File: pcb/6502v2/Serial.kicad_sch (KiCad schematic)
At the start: 10 parts

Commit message: Finally figured out the address decode logic, hopefully im done for now
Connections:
- net A0: now also U?.13 (RS0)
- net A1: now also U?.14 (RS1)
- net Serial Enable: now reaches U?.2 (CS1)
- net Serial ~{Enable}: now reaches U?.3 (~{CS2})
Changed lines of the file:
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@@
     (effects (font (size 1.27 1.27)) (justify right))
   )
-  (hierarchical_label "A1" (shape input) (at 165.354 62.738 180)
+  (hierarchical_label "A1" (shape input) (at 187.706 65.786 180)
+    (effects (font (size 1.27 1.27)) (justify right))
+  )
+  (hierarchical_label "Serial ~{Enable}" (shape input) (at 187.706 58.166 180)
     (effects (font (size 1.27 1.27)) (justify right))
   )
@@
     (effects (font (size 1.27 1.27)) (justify right))
   )
-  (hierarchical_label "A2" (shape input) (at 165.354 65.278 180)
+  (hierarchical_label "Serial Enable" (shape input) (at 187.706 55.626 180)
     (effects (font (size 1.27 1.27)) (justify right))
   )
@@
     (effects (font (size 1.27 1.27)) (justify right))
   )
-  (hierarchical_label "A3" (shape input) (at 165.354 67.818 180)
-    (effects (font (size 1.27 1.27)) (justify right))
-  )
   (hierarchical_label "D5" (shape bidirectional) (at 187.706 93.726 180)
     (effects (font (size 1.27 1.27)) (justify right))
   )
-  (hierarchical_label "A0" (shape input) (at 165.354 60.198 180)
+  (hierarchical_label "A0" (shape input) (at 187.706 63.246 180)
     (effects (font (size 1.27 1.27)) (justify right))
   )
@@
   (symbol (lib_id "power:GND") (at 107.95 113.284 0) (unit 1)
     (in_bom yes) (on_board yes) (fields_autoplaced)
-    (property "Reference" "#PWR?" (id 0) (at 107.95 119.634 0)
+    (property "Reference" "#PWR0145" (id 0) (at 107.95 119.634 0)
       (effects (font (size 1.27 1.27)) hide)
     )
@@
   (symbol (lib_id "power:GND") (at 31.496 87.376 0) (unit 1)
     (in_bom yes) (on_board yes) (fields_autoplaced)
-    (property "Reference" "#PWR?" (id 0) (at 31.496 93.726 0)
+    (property "Reference" "#PWR0144" (id 0) (at 31.496 93.726 0)
       (effects (font (size 1.27 1.27)) hide)
     )
@@
   (symbol (lib_id "power:GND") (at 248.666 42.926 0) (unit 1)
     (in_bom yes) (on_board yes) (fields_autoplaced)
-    (property "Reference" "#PWR?" (id 0) (at 248.666 49.276 0)
+    (property "Reference" "#PWR0147" (id 0) (at 248.666 49.276 0)
       (effects (font (size 1.27 1.27)) hide)
     )
@@
   (symbol (lib_id "power:GND") (at 202.946 108.966 0) (unit 1)
     (in_bom yes) (on_board yes) (fields_autoplaced)
-    (property "Reference" "#PWR?" (id 0) (at 202.946 115.316 0)
+    (property "Reference" "#PWR0148" (id 0) (at 202.946 115.316 0)
       (effects (font (size 1.27 1.27)) hide)
     )
@@
   (symbol (lib_id "power:+5V") (at 202.946 32.258 0) (unit 1)
     (in_bom yes) (on_board yes) (fields_autoplaced)
-    (property "Reference" "#PWR?" (id 0) (at 202.946 36.068 0)
+    (property "Reference" "#PWR0146" (id 0) (at 202.946 36.068 0)
       (effects (font (size 1.27 1.27)) hide)
     )
@@
   (symbol (lib_id "power:GND") (at 141.224 85.344 0) (unit 1)
     (in_bom yes) (on_board yes) (fields_autoplaced)
-    (property "Reference" "#PWR?" (id 0) (at 141.224 91.694 0)
+    (property "Reference" "#PWR0142" (id 0) (at 141.224 91.694 0)
       (effects (font (size 1.27 1.27)) hide)
     )
@@
   (symbol (lib_id "power:+5V") (at 107.95 51.054 0) (unit 1)
     (in_bom yes) (on_board yes) (fields_autoplaced)
-    (property "Reference" "#PWR?" (id 0) (at 107.95 54.864 0)
-      (effects (font (size 1.27 1.27)) hide)
-    )
+    (property "Reference" "#PWR0143" (id 0) (at 107.95 54.864 0)
+      (effects (font (size 1.27 1.27)) hide)
+    )

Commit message: just working
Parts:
- C1, C2, C3, C4, C5: renamed from C?; footprint (none) -> Capacitor_SMD:C_0805_2012Metric
- J12: renamed from J?; footprint (none) -> Connector_Dsub:DSUB-9_Female_Horizontal_P2.77x2.84mm_EdgePinOffset4.94mm_Housed_MountingHolesOffset7.48mm
- R33: renamed from R?; footprint (none) -> Resistor_SMD:R_0805_2012Metric
- U7: renamed from U?; footprint (none) -> Package_DIP:DIP-16_W7.62mm
- Y1: renamed from Y?; footprint (none) -> Crystal:Crystal_HC49-U_Vertical
- gave numbers to parts that had none: 1
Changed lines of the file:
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@@
   (symbol (lib_id "Device:C_Small") (at 132.334 63.754 0) (unit 1)
     (in_bom yes) (on_board yes) (fields_autoplaced)
-    (property "Reference" "C?" (id 0) (at 135.89 62.4902 0)
+    (property "Reference" "C2" (id 0) (at 135.89 62.4902 0)
       (effects (font (size 1.27 1.27)) (justify left))
     )
@@
       (effects (font (size 1.27 1.27)) (justify left))
     )
-    (property "Footprint" "" (id 2) (at 132.334 63.754 0)
+    (property "Footprint" "Capacitor_SMD:C_0805_2012Metric" (id 2) (at 132.334 63.754 0)
       (effects (font (size 1.27 1.27)) hide)
     )
@@
   (symbol (lib_id "Device:R_Small") (at 224.028 43.942 0) (unit 1)
     (in_bom yes) (on_board yes)
-    (property "Reference" "R?" (id 0) (at 226.06 42.6719 0)
+    (property "Reference" "R33" (id 0) (at 226.06 42.6719 0)
       (effects (font (size 1.27 1.27)) (justify left))
     )
@@
       (effects (font (size 1.27 1.27)) (justify left))
     )
-    (property "Footprint" "" (id 2) (at 224.028 43.942 0)
+    (property "Footprint" "Resistor_SMD:R_0805_2012Metric" (id 2) (at 224.028 43.942 0)
       (effects (font (size 1.27 1.27)) hide)
     )
@@
   (symbol (lib_id "power:GND") (at 107.95 113.284 0) (unit 1)
     (in_bom yes) (on_board yes) (fields_autoplaced)
-    (property "Reference" "#PWR0145" (id 0) (at 107.95 119.634 0)
+    (property "Reference" "#PWR044" (id 0) (at 107.95 119.634 0)
       (effects (font (size 1.27 1.27)) hide)
     )
@@
   (symbol (lib_id "power:GND") (at 31.496 87.376 0) (unit 1)
     (in_bom yes) (on_board yes) (fields_autoplaced)
-    (property "Reference" "#PWR0144" (id 0) (at 31.496 93.726 0)
+    (property "Reference" "#PWR042" (id 0) (at 31.496 93.726 0)
       (effects (font (size 1.27 1.27)) hide)
     )
@@
   (symbol (lib_id "Device:C_Small") (at 141.224 75.184 0) (unit 1)
     (in_bom yes) (on_board yes) (fields_autoplaced)
-    (property "Reference" "C?" (id 0) (at 144.78 73.9202 0)
+    (property "Reference" "C4" (id 0) (at 144.78 73.9202 0)
       (effects (font (size 1.27 1.27)) (justify left))
     )
@@
       (effects (font (size 1.27 1.27)) (justify left))
     )
-    (property "Footprint" "" (id 2) (at 141.224 75.184 0)
+    (property "Footprint" "Capacitor_SMD:C_0805_2012Metric" (id 2) (at 141.224 75.184 0)
       (effects (font (size 1.27 1.27)) hide)
     )
@@
   (symbol (lib_id "Device:C_Small") (at 248.666 38.862 0) (unit 1)
     (in_bom yes) (on_board yes) (fields_autoplaced)
-    (property "Reference" "C?" (id 0) (at 252.222 37.5982 0)
+    (property "Reference" "C5" (id 0) (at 252.222 37.5982 0)
       (effects (font (size 1.27 1.27)) (justify left))
     )
@@
       (effects (font (size 1.27 1.27)) (justify left))
     )
-    (property "Footprint" "" (id 2) (at 248.666 38.862 0)
+    (property "Footprint" "Capacitor_SMD:C_0805_2012Metric" (id 2) (at 248.666 38.862 0)
       (effects (font (size 1.27 1.27)) hide)
     )
@@
   (symbol (lib_id "Device:C_Small") (at 138.684 82.804 0) (unit 1)
     (in_bom yes) (on_board yes) (fields_autoplaced)
-    (property "Reference" "C?" (id 0) (at 142.24 81.5402 0)
+    (property "Reference" "C3" (id 0) (at 142.24 81.5402 0)
       (effects (font (size 1.27 1.27)) (justify left))
     )
@@
       (effects (font (size 1.27 1.27)) (justify left))
     )
-    (property "Footprint" "" (id 2) (at 138.684 82.804 0)
+    (property "Footprint" "Capacitor_SMD:C_0805_2012Metric" (id 2) (at 138.684 82.804 0)
       (effects (font (size 1.27 1.27)) hide)
     )
@@
   (symbol (lib_id "Device:C_Small") (at 80.264 63.246 0) (unit 1)
     (in_bom yes) (on_board yes) (fields_autoplaced)
-    (property "Reference" "C?" (id 0) (at 83.82 61.9822 0)
+    (property "Reference" "C1" (id 0) (at 83.82 61.9822 0)
       (effects (font (size 1.27 1.27)) (justify left))
     )
@@
       (effects (font (size 1.27 1.27)) (justify left))
     )
-    (property "Footprint" "" (id 2) (at 80.264 63.246 0)
+    (property "Footprint" "Capacitor_SMD:C_0805_2012Metric" (id 2) (at 80.264 63.246 0)
       (effects (font (size 1.27 1.27)) hide)
     )
@@
   (symbol (lib_id "65xx:W65C51NxP") (at 202.946 70.866 0) (unit 1)
     (in_bom yes) (on_board yes) (fields_autoplaced)
-    (property "Reference" "U?" (id 0) (at 204.9654 34.544 0)
+    (property "Reference" "U8" (id 0) (at 204.9654 34.544 0)
       (effects (font (size 1.27 1.27)) (justify left))
     )
@@
   (symbol (lib_id "Device:Crystal_Small") (at 232.41 43.688 90) (unit 1)
     (in_bom yes) (on_board yes) (fields_autoplaced)
-    (property "Reference" "Y?" (id 0) (at 234.95 42.4179 90)
+    (property "Reference" "Y1" (id 0) (at 234.95 42.4179 90)
       (effects (font (size 1.27 1.27)) (justify right))
     )
@@
       (effects (font (size 1.27 1.27)) (justify right))
     )
-    (property "Footprint" "" (id 2) (at 232.41 43.688 0)
+    (property "Footprint" "Crystal:Crystal_HC49-U_Vertical" (id 2) (at 232.41 43.688 0)
       (effects (font (size 1.27 1.27)) hide)
     )
@@
   (symbol (lib_id "Interface_UART:MAX232") (at 107.95 82.804 0) (unit 1)
     (in_bom yes) (on_board yes) (fields_autoplaced)
-    (property "Reference" "U?" (id 0) (at 109.9694 51.562 0)
+    (property "Reference" "U7" (id 0) (at 109.9694 51.562 0)
       (effects (font (size 1.27 1.27)) (justify left))
     )
@@
       (effects (font (size 1.27 1.27)) (justify left))
     )
-    (property "Footprint" "" (id 2) (at 109.22 109.474 0)
+    (property "Footprint" "Package_DIP:DIP-16_W7.62mm" (id 2) (at 109.22 109.474 0)
       (effects (font (size 1.27 1.27)) (justify left) hide)
     )
@@
   (symbol (lib_id "power:GND") (at 248.666 42.926 0) (unit 1)
     (in_bom yes) (on_board yes) (fields_autoplaced)
-    (property "Reference" "#PWR0147" (id 0) (at 248.666 49.276 0)
+    (property "Reference" "#PWR048" (id 0) (at 248.666 49.276 0)
       (effects (font (size 1.27 1.27)) hide)
     )
@@
   (symbol (lib_id "power:GND") (at 202.946 108.966 0) (unit 1)
     (in_bom yes) (on_board yes) (fields_autoplaced)
-    (property "Reference" "#PWR0148" (id 0) (at 202.946 115.316 0)
+    (property "Reference" "#PWR047" (id 0) (at 202.946 115.316 0)
       (effects (font (size 1.27 1.27)) hide)
     )
@@
   (symbol (lib_id "power:+5V") (at 202.946 32.258 0) (unit 1)
     (in_bom yes) (on_board yes) (fields_autoplaced)
-    (property "Reference" "#PWR0146" (id 0) (at 202.946 36.068 0)
+    (property "Reference" "#PWR046" (id 0) (at 202.946 36.068 0)
       (effects (font (size 1.27 1.27)) hide)
     )
@@
   (symbol (lib_id "power:GND") (at 141.224 85.344 0) (unit 1)
     (in_bom yes) (on_board yes) (fields_autoplaced)
-    (property "Reference" "#PWR0142" (id 0) (at 141.224 91.694 0)
+    (property "Reference" "#PWR045" (id 0) (at 141.224 91.694 0)
       (effects (font (size 1.27 1.27)) hide)
     )
@@
   (symbol (lib_id "power:+5V") (at 107.95 51.054 0) (unit 1)
     (in_bom yes) (on_board yes) (fields_autoplaced)
-    (property "Reference" "#PWR0143" (id 0) (at 107.95 54.864 0)
+    (property "Reference" "#PWR043" (id 0) (at 107.95 54.864 0)
       (effects (font (size 1.27 1.27)) hide)
     )
@@
   (symbol (lib_id "Connector:DB9_Female") (at 40.894 77.216 0) (unit 1)
     (in_bom yes) (on_board yes) (fields_autoplaced)
-    (property "Reference" "J?" (id 0) (at 45.466 75.9459 0)
+    (property "Reference" "J12" (id 0) (at 45.466 75.9459 0)
       (effects (font (size 1.27 1.27)) (justify left))
     )
@@
       (effects (font (size 1.27 1.27)) (justify left))
     )
-    (property "Footprint" "" (id 2) (at 40.894 77.216 0)
-      (effects (font (size 1.27 1.27)) hide)
-    )
+    (property "Footprint" "Connector_Dsub:DSUB-9_Female_Horizontal_P2.77x2.84mm_EdgePinOffset4.94mm_Housed_MountingHolesOffset7.48mm" (id 2) (at 40.894 77.216 0)
+      (effects (font (size 1.27 1.27)) hide)
+    )

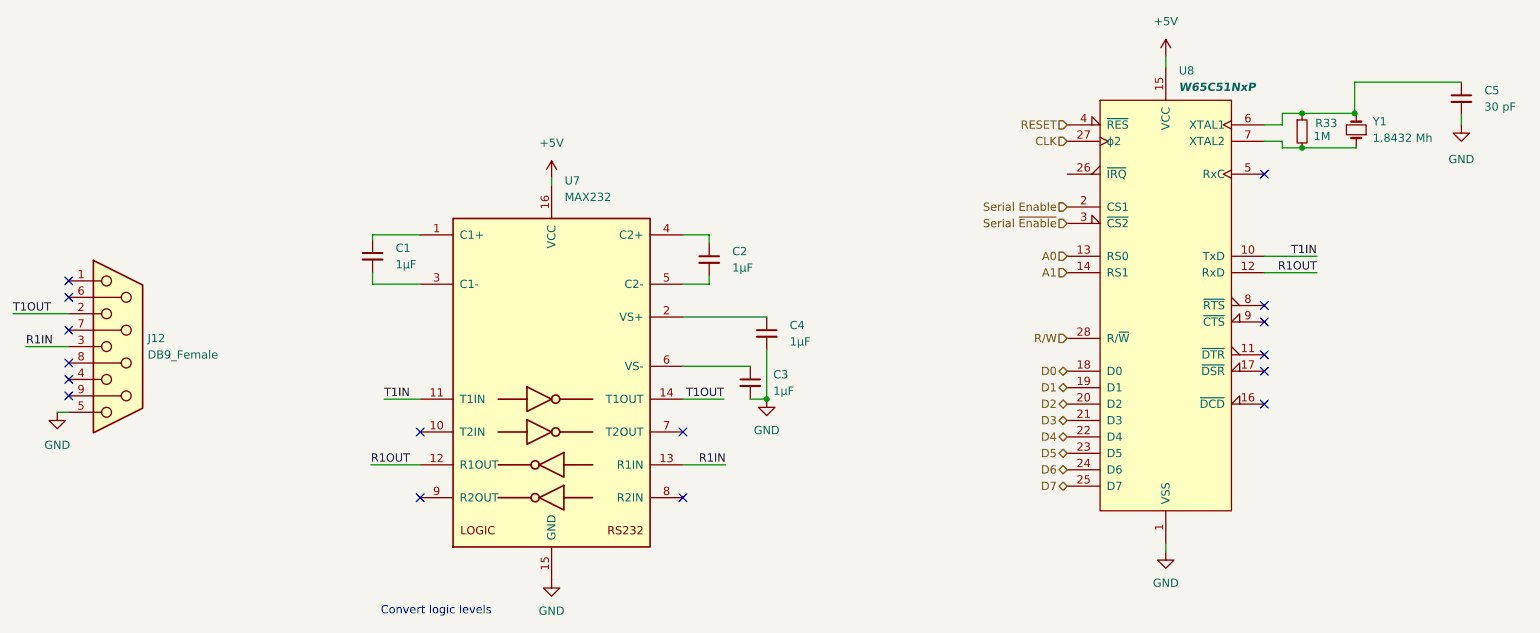
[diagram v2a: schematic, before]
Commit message: Yo yo yo i make the bord 102 by 102 cause jlc pricing
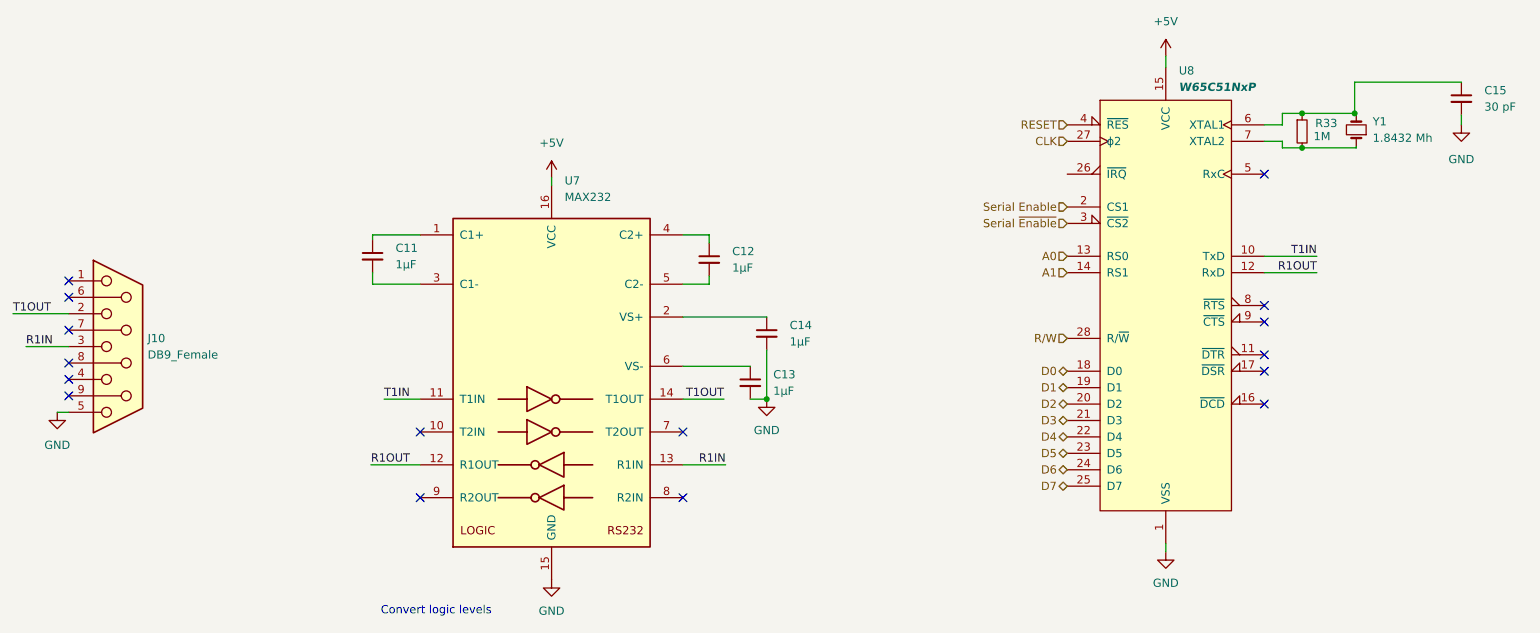
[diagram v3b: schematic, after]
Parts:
- renumbered C1 to C11, C2 to C12, C3 to C13, C4 to C14, C5 to C15, J12 to J10
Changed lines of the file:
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@@
   (symbol (lib_id "Device:C_Small") (at 132.334 63.754 0) (unit 1)
     (in_bom yes) (on_board yes) (fields_autoplaced)
-    (property "Reference" "C2" (id 0) (at 135.89 62.4902 0)
+    (property "Reference" "C12" (id 0) (at 135.89 62.4902 0)
       (effects (font (size 1.27 1.27)) (justify left))
     )
@@
   (symbol (lib_id "power:GND") (at 107.95 113.284 0) (unit 1)
     (in_bom yes) (on_board yes) (fields_autoplaced)
-    (property "Reference" "#PWR044" (id 0) (at 107.95 119.634 0)
+    (property "Reference" "#PWR046" (id 0) (at 107.95 119.634 0)
       (effects (font (size 1.27 1.27)) hide)
     )
@@
   (symbol (lib_id "power:GND") (at 31.496 87.376 0) (unit 1)
     (in_bom yes) (on_board yes) (fields_autoplaced)
-    (property "Reference" "#PWR042" (id 0) (at 31.496 93.726 0)
+    (property "Reference" "#PWR044" (id 0) (at 31.496 93.726 0)
       (effects (font (size 1.27 1.27)) hide)
     )
@@
   (symbol (lib_id "Device:C_Small") (at 141.224 75.184 0) (unit 1)
     (in_bom yes) (on_board yes) (fields_autoplaced)
-    (property "Reference" "C4" (id 0) (at 144.78 73.9202 0)
+    (property "Reference" "C14" (id 0) (at 144.78 73.9202 0)
       (effects (font (size 1.27 1.27)) (justify left))
     )
@@
   (symbol (lib_id "Device:C_Small") (at 248.666 38.862 0) (unit 1)
     (in_bom yes) (on_board yes) (fields_autoplaced)
-    (property "Reference" "C5" (id 0) (at 252.222 37.5982 0)
+    (property "Reference" "C15" (id 0) (at 252.222 37.5982 0)
       (effects (font (size 1.27 1.27)) (justify left))
     )
@@
   (symbol (lib_id "Device:C_Small") (at 138.684 82.804 0) (unit 1)
     (in_bom yes) (on_board yes) (fields_autoplaced)
-    (property "Reference" "C3" (id 0) (at 142.24 81.5402 0)
+    (property "Reference" "C13" (id 0) (at 142.24 81.5402 0)
       (effects (font (size 1.27 1.27)) (justify left))
     )
@@
   (symbol (lib_id "Device:C_Small") (at 80.264 63.246 0) (unit 1)
     (in_bom yes) (on_board yes) (fields_autoplaced)
-    (property "Reference" "C1" (id 0) (at 83.82 61.9822 0)
+    (property "Reference" "C11" (id 0) (at 83.82 61.9822 0)
       (effects (font (size 1.27 1.27)) (justify left))
     )
@@
   (symbol (lib_id "power:GND") (at 248.666 42.926 0) (unit 1)
     (in_bom yes) (on_board yes) (fields_autoplaced)
-    (property "Reference" "#PWR048" (id 0) (at 248.666 49.276 0)
+    (property "Reference" "#PWR050" (id 0) (at 248.666 49.276 0)
       (effects (font (size 1.27 1.27)) hide)
     )
@@
   (symbol (lib_id "power:GND") (at 202.946 108.966 0) (unit 1)
     (in_bom yes) (on_board yes) (fields_autoplaced)
-    (property "Reference" "#PWR047" (id 0) (at 202.946 115.316 0)
+    (property "Reference" "#PWR049" (id 0) (at 202.946 115.316 0)
       (effects (font (size 1.27 1.27)) hide)
     )
@@
   (symbol (lib_id "power:+5V") (at 202.946 32.258 0) (unit 1)
     (in_bom yes) (on_board yes) (fields_autoplaced)
-    (property "Reference" "#PWR046" (id 0) (at 202.946 36.068 0)
+    (property "Reference" "#PWR048" (id 0) (at 202.946 36.068 0)
       (effects (font (size 1.27 1.27)) hide)
     )
@@
   (symbol (lib_id "power:GND") (at 141.224 85.344 0) (unit 1)
     (in_bom yes) (on_board yes) (fields_autoplaced)
-    (property "Reference" "#PWR045" (id 0) (at 141.224 91.694 0)
+    (property "Reference" "#PWR047" (id 0) (at 141.224 91.694 0)
       (effects (font (size 1.27 1.27)) hide)
     )
@@
   (symbol (lib_id "power:+5V") (at 107.95 51.054 0) (unit 1)
     (in_bom yes) (on_board yes) (fields_autoplaced)
-    (property "Reference" "#PWR043" (id 0) (at 107.95 54.864 0)
+    (property "Reference" "#PWR045" (id 0) (at 107.95 54.864 0)
       (effects (font (size 1.27 1.27)) hide)
     )
@@
   (symbol (lib_id "Connector:DB9_Female") (at 40.894 77.216 0) (unit 1)
     (in_bom yes) (on_board yes) (fields_autoplaced)
-    (property "Reference" "J12" (id 0) (at 45.466 75.9459 0)
-      (effects (font (size 1.27 1.27)) (justify left))
-    )
+    (property "Reference" "J10" (id 0) (at 45.466 75.9459 0)
+      (effects (font (size 1.27 1.27)) (justify left))
+    )
